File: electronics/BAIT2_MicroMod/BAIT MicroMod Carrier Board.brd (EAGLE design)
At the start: 92.7 x 80 mm, 147 parts, among them J1 SJ-43516-SMT, J10 QWIIC_RIGHT_ANGLE, J15 SM06B-SRSS-TB(LF)(SN), J2 ST-TF-003A, J4 JST_6_PIN_VERTICAL, J5 QWIIC_RIGHT_ANGLE, J6 JST 2PH, J7 MICROMOD-2222-C, SW1 SKQGADE010, SW2 SKQGADE010, U1 SGTL5000-32, U10 TSL25911, U2 AP7313, U3 3.3V, U4 3.3V, U5 BQ27441-G1, U6 BQ24074, U7 LoRa-E5-HF, U8 S-1172B33-E6T1U, U9 BOSCH_TOOLS_BME680BOSCH_TOOLS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

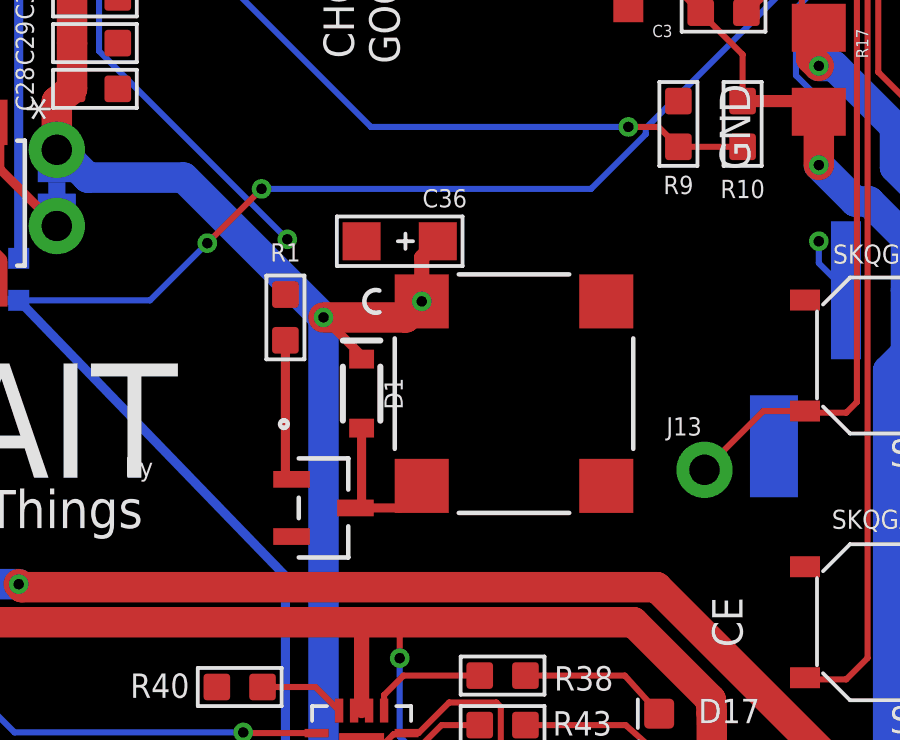
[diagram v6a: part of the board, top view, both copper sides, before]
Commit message: Removes testing buzzer
Resolves #21 and partially #14
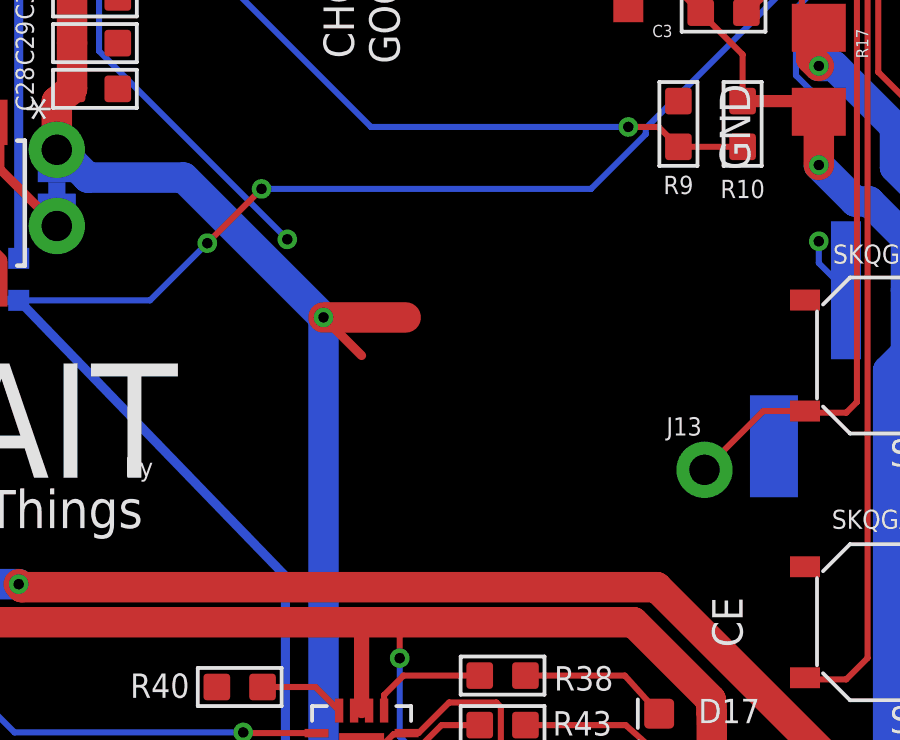
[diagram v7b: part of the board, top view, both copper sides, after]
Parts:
- removed C36: 10uf, OPL_Capacitor:AVX-A
- removed D1: 250mA/100V, SparkFun-DiscreteSemi:SOD-323
- removed LS1: CMT-7525-80-SMT-TRCMT-7525-80-SMT-TR_CUD, 2022-07-25_09-48-13_Library:CMT-7525-80-SMT-TR_CUD
- removed R1: 200K, OPL_Resistor:R0603
- removed TR1: MMBT2222A-TPMTR_MMBT2222A-TP_MCE, 2022-07-25_10-23-18_Library:MTR_MMBT2222A-TP_MCE
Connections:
- removed net N$1: R1.2, TR1.1
- removed net N$2: D1.A, LS1.2, TR1.3
- net 3.3V: no longer C36.+, D1.C, LS1.1
- net GND: no longer C36.-, TR1.2
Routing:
- net N$2: track 5.26 -> 0.00 mm
- net N$1: track 4.72 -> 0.00 mm
- net 3.3V: track 271.8 -> 268.7 mm, vias 13 -> 12

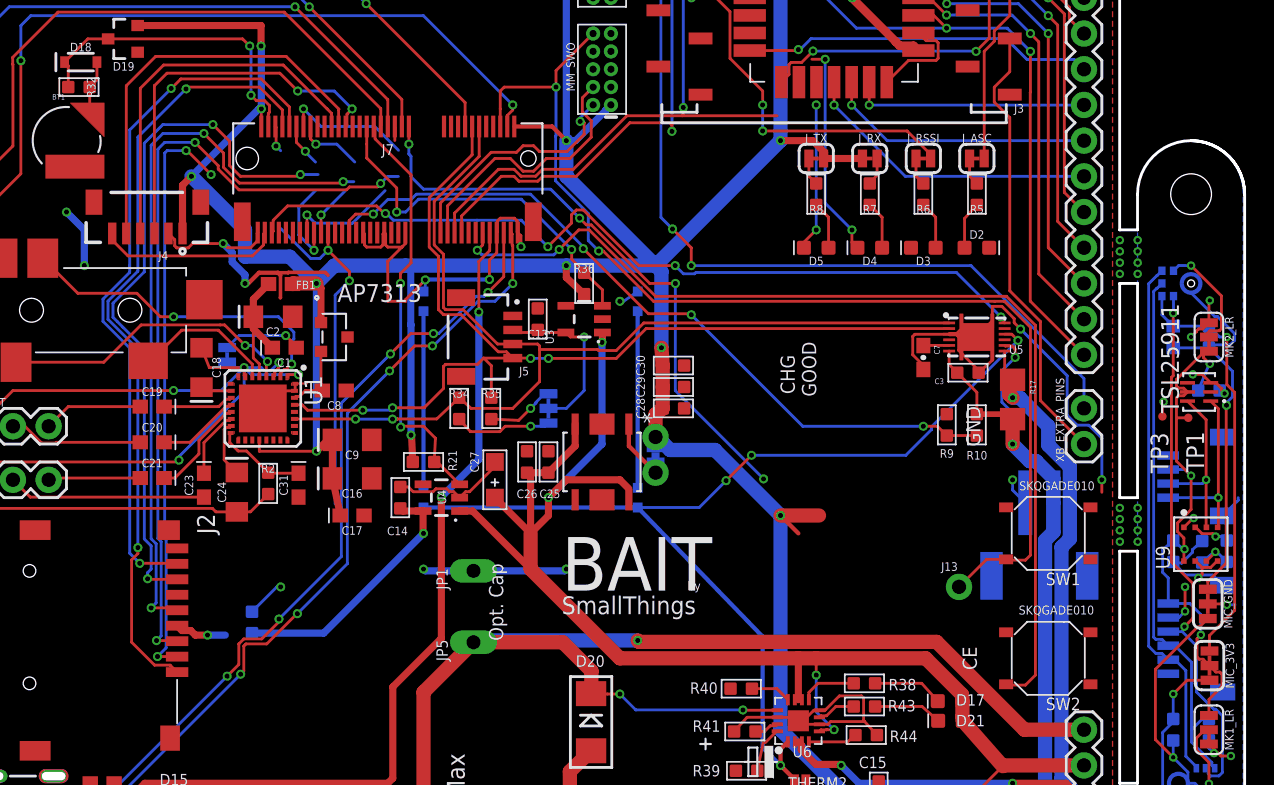
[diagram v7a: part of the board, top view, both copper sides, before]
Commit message: Updated the JST connectors
Switched to the correct (vertical orientation) connector and swapped the 6-pin audio connector for a 5-pin version
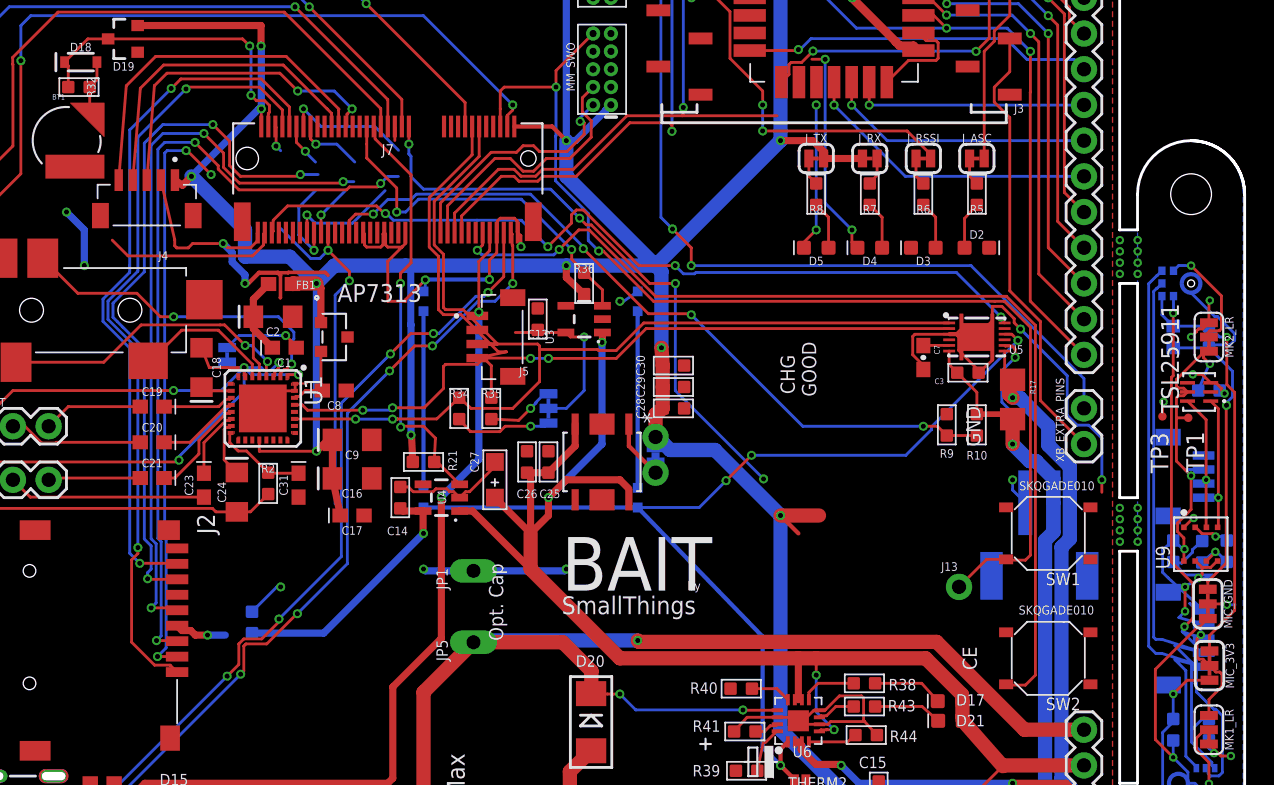
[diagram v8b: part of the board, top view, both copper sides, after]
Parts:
- J10: device SM04B-SRSS-TB_LF__SN_:JST_SM04B-SRSS-TB(LF)(SN) -> JST SH Connectors:JST_BM04B-SRSS-TB(LF)(SN)
- J15: value SM06B-SRSS-TB(LF)(SN) -> BM05B-SRSS-TB(LF)(SN); device SM06B-SRSS-TB_LF__SN_:JST_SM06B-SRSS-TB(LF)(SN) -> JST SH Connectors:JST_BM05B-SRSS-TB(LF)(SN)
- J4: value JST_6_PIN_VERTICAL -> BM05B-SRSS-TB(LF)(SN); device SparkFun-Connectors:JST-6-SMD-VERT-1.0MM -> JST SH Connectors:JST_BM05B-SRSS-TB(LF)(SN)
- J5: device SparkFun-Connectors:JST04_1MM_RA -> JST SH Connectors:JST_BM04B-SRSS-TB(LF)(SN)
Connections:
- net GND: now also J5.S1, J5.S2
- net LR_SEL: no longer J4.6
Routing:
- net WS_B: track 37.7 -> 41.8 mm
- net SD_B: track 38.6 -> 42.8 mm
- net I2S_WS: track 29.3 -> 25.5 mm
- net I2S_SCK: track 27.4 -> 23.7 mm
- net I2S_SD: track 27.0 -> 23.2 mm
- net GND: track 153.4 -> 157.2 mm
- net I2C_SDA: track 74.1 -> 77.0 mm
- net 3.3V: track 268.7 -> 265.9 mm
- net SCL_B: track 12.8 -> 10.3 mm
- net I2C_SCL: track 74.4 -> 76.8 mm
- net SDA_B: track 12.4 -> 10.0 mm
- net GND_B: track 28.8 -> 30.4 mm
- net 3V3_B: track 41.8 -> 43.2 mm
- net SCK_B: track 38.8 -> 39.4 mm
